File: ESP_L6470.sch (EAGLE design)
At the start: 39 parts, among them IC2 CP2104, J1 MICRO-USB, J2 POWER_JACKPTH_LOCK, J3 ENCODER, J4 ENDSTOP2, J5 ENDSTOP1, J6 STEPER, Q1 600mA/40V, Q2 600mA/40V, U1 L6470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

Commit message: renamed aesthetics
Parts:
- renumbered U$13 to A2, U$15 to A1
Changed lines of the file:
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@@
 <part name="R11" library="SparkFun-Passives" deviceset="RESISTOR" device="0603-RES" value="1k"/>
 <part name="R12" library="SparkFun-Passives" deviceset="RESISTOR" device="0603-RES" value="1k"/>
-<part name="U$13" library="IAD_GRAPHIC" deviceset="INTERFACE_NETSTEPPER" device=""/>
-<part name="U$15" library="IAD_GRAPHIC" deviceset="ZHDK_LOGO_METAL" device=""/>
+<part name="A2" library="IAD_GRAPHIC" deviceset="INTERFACE_NETSTEPPER" device=""/>
+<part name="A1" library="IAD_GRAPHIC" deviceset="ZHDK_LOGO_METAL" device=""/>
 </parts>
 <sheets>
@@
 <instance part="R11" gate="G$1" x="279.4" y="99.06"/>
 <instance part="R12" gate="G$1" x="279.4" y="91.44"/>
-<instance part="U$13" gate="G$1" x="251.46" y="127"/>
-<instance part="U$15" gate="G$1" x="254" y="134.62"/>
+<instance part="A2" gate="G$1" x="251.46" y="127"/>
+<instance part="A1" gate="G$1" x="254" y="134.62"/>
 </instances>
 <busses>

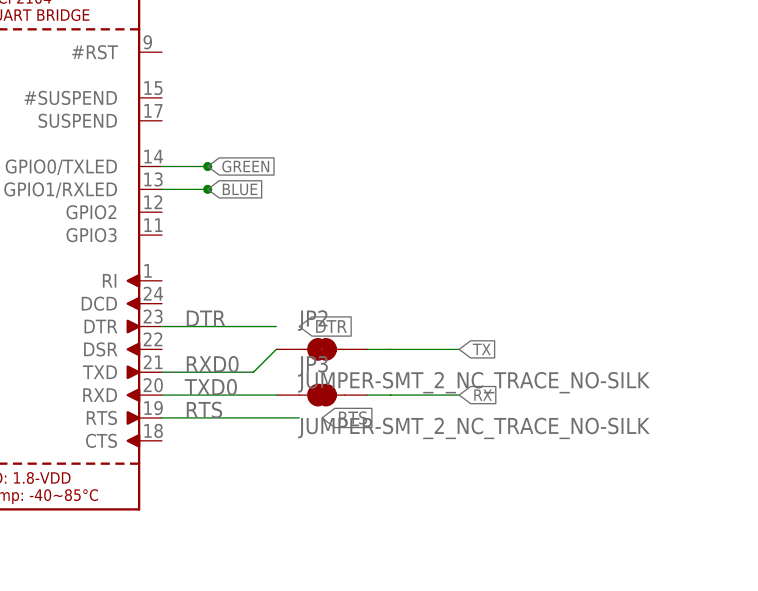
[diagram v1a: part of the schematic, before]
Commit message: fixed tx and rx pins and removed jumpers
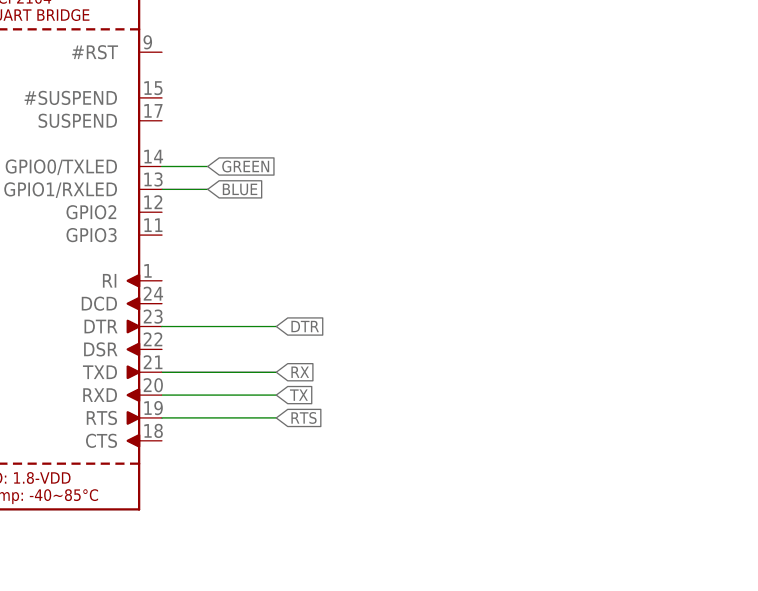
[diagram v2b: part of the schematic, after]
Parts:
- removed JP2, JP3: JUMPER-SMT_2_NC_TRACE_NO-SILK, SparkFun-Jumpers:JUMPER-SMT_2_NC_TRACE_NO-SILK
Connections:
- removed net RXD0: IC2G$1.TXD, JP2.1
- removed net TXD0: IC2G$1.RXD, JP3.1
- net RX: now also IC2G$1.TXD; no longer JP3.2
- net TX: now also IC2G$1.RXD; no longer JP2.2
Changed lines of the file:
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@@
 <part name="U$36" library="microbuilder" deviceset="VBUS" device=""/>
 <part name="U$38" library="microbuilder" deviceset="3.3V" device=""/>
-<part name="JP2" library="SparkFun-Jumpers" deviceset="JUMPER-SMT_2_NC_TRACE" device="_NO-SILK"/>
-<part name="JP3" library="SparkFun-Jumpers" deviceset="JUMPER-SMT_2_NC_TRACE" device="_NO-SILK"/>
 <part name="J1" library="SparkFun-Connectors" deviceset="USB_MICRO-B" device="_SMT" value="MICRO-USB"/>
 <part name="U3" library="Particle" deviceset="RGB-LED-CLMVB-FKA" device="RGB" value="RGB-LED"/>
@@
 <instance part="U$36" gate="G$1" x="401.32" y="40.64"/>
 <instance part="U$38" gate="G$1" x="403.86" y="58.42"/>
-<instance part="JP2" gate="G$1" x="464.82" y="27.94"/>
-<instance part="JP3" gate="G$1" x="464.82" y="22.86"/>
 <instance part="J1" gate="G$1" x="383.54" y="33.02" rot="R180"/>
 <instance part="U3" gate="G$1" x="259.08" y="99.06" rot="R90"/>
@@
 <pinref part="IC2" gate="G$1" pin="DTR"/>
 <wire x1="447.04" y1="30.48" x2="459.74" y2="30.48" width="0.1524" layer="91"/>
-<label x="449.58" y="30.48" size="1.778" layer="95"/>
-<label x="462.28" y="30.48" size="1.4224" layer="95" xref="yes"/>
+<label x="459.74" y="30.48" size="1.27" layer="95" xref="yes"/>
 </segment>
 </net>
@@
 </segment>
 <segment>
-<wire x1="462.28" y1="20.32" x2="447.04" y2="20.32" width="0.1524" layer="91"/>
+<wire x1="459.74" y1="20.32" x2="447.04" y2="20.32" width="0.1524" layer="91"/>
 <pinref part="IC2" gate="G$1" pin="RTS"/>
-<label x="449.58" y="20.32" size="1.778" layer="95"/>
-<label x="464.82" y="20.32" size="1.4224" layer="95" xref="yes"/>
+<label x="459.74" y="20.32" size="1.27" layer="95" xref="yes"/>
 </segment>
 </net>
@@
 </segment>
 <segment>
-<label x="480.06" y="27.94" size="1.27" layer="95" xref="yes"/>
-<wire x1="472.44" y1="27.94" x2="480.06" y2="27.94" width="0.1524" layer="91"/>
-<pinref part="JP2" gate="G$1" pin="2"/>
-<wire x1="472.44" y1="27.94" x2="469.9" y2="27.94" width="0.1524" layer="91"/>
+<pinref part="IC2" gate="G$1" pin="RXD"/>
+<wire x1="447.04" y1="22.86" x2="459.74" y2="22.86" width="0.1524" layer="91"/>
+<label x="459.74" y="22.86" size="1.27" layer="95" xref="yes"/>
 </segment>
 </net>
@@
 </segment>
 <segment>
-<label x="480.06" y="22.86" size="1.27" layer="95" xref="yes"/>
-<wire x1="472.44" y1="22.86" x2="480.06" y2="22.86" width="0.1524" layer="91"/>
-<pinref part="JP3" gate="G$1" pin="2"/>
-<wire x1="472.44" y1="22.86" x2="469.9" y2="22.86" width="0.1524" layer="91"/>
+<pinref part="IC2" gate="G$1" pin="TXD"/>
+<wire x1="447.04" y1="25.4" x2="459.74" y2="25.4" width="0.1524" layer="91"/>
+<label x="459.74" y="25.4" size="1.27" layer="95" xref="yes"/>
 </segment>
 </net>
@@
 </segment>
 </net>
-<net name="RXD0" class="0">
-<segment>
-<wire x1="447.04" y1="25.4" x2="457.2" y2="25.4" width="0.1524" layer="91"/>
-<wire x1="457.2" y1="25.4" x2="459.74" y2="27.94" width="0.1524" layer="91"/>
-<pinref part="IC2" gate="G$1" pin="TXD"/>
-<label x="449.58" y="25.4" size="1.778" layer="95"/>
-<pinref part="JP2" gate="G$1" pin="1"/>
-</segment>
-</net>
-<net name="TXD0" class="0">
-<segment>
-<wire x1="459.74" y1="22.86" x2="447.04" y2="22.86" width="0.1524" layer="91"/>
-<pinref part="IC2" gate="G$1" pin="RXD"/>
-<label x="449.58" y="22.86" size="1.778" layer="95"/>
-<pinref part="JP3" gate="G$1" pin="1"/>
-</segment>
-</net>
 <net name="N$13" class="0">
 <segment>
@@
 <pinref part="IC2" gate="G$1" pin="GPIO0/TXLED"/>
 <wire x1="447.04" y1="48.26" x2="452.12" y2="48.26" width="0.1524" layer="91"/>
-<junction x="452.12" y="48.26"/>
 </segment>
 </net>
@@
 <pinref part="IC2" gate="G$1" pin="GPIO1/RXLED"/>
 <wire x1="447.04" y1="45.72" x2="452.12" y2="45.72" width="0.1524" layer="91"/>
-<junction x="452.12" y="45.72"/>
-</segment>
-</net>
+</segment>
+</net>
